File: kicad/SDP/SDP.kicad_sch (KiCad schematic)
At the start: 83 parts, among them J1 GPIO, J2 SPI, J24 POWER, J3 UART, J4 I2C, J5 Conn_01x04, J6 Conn_01x04, J7 RJ25, SW1 SW_Push, U1 TPS54233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

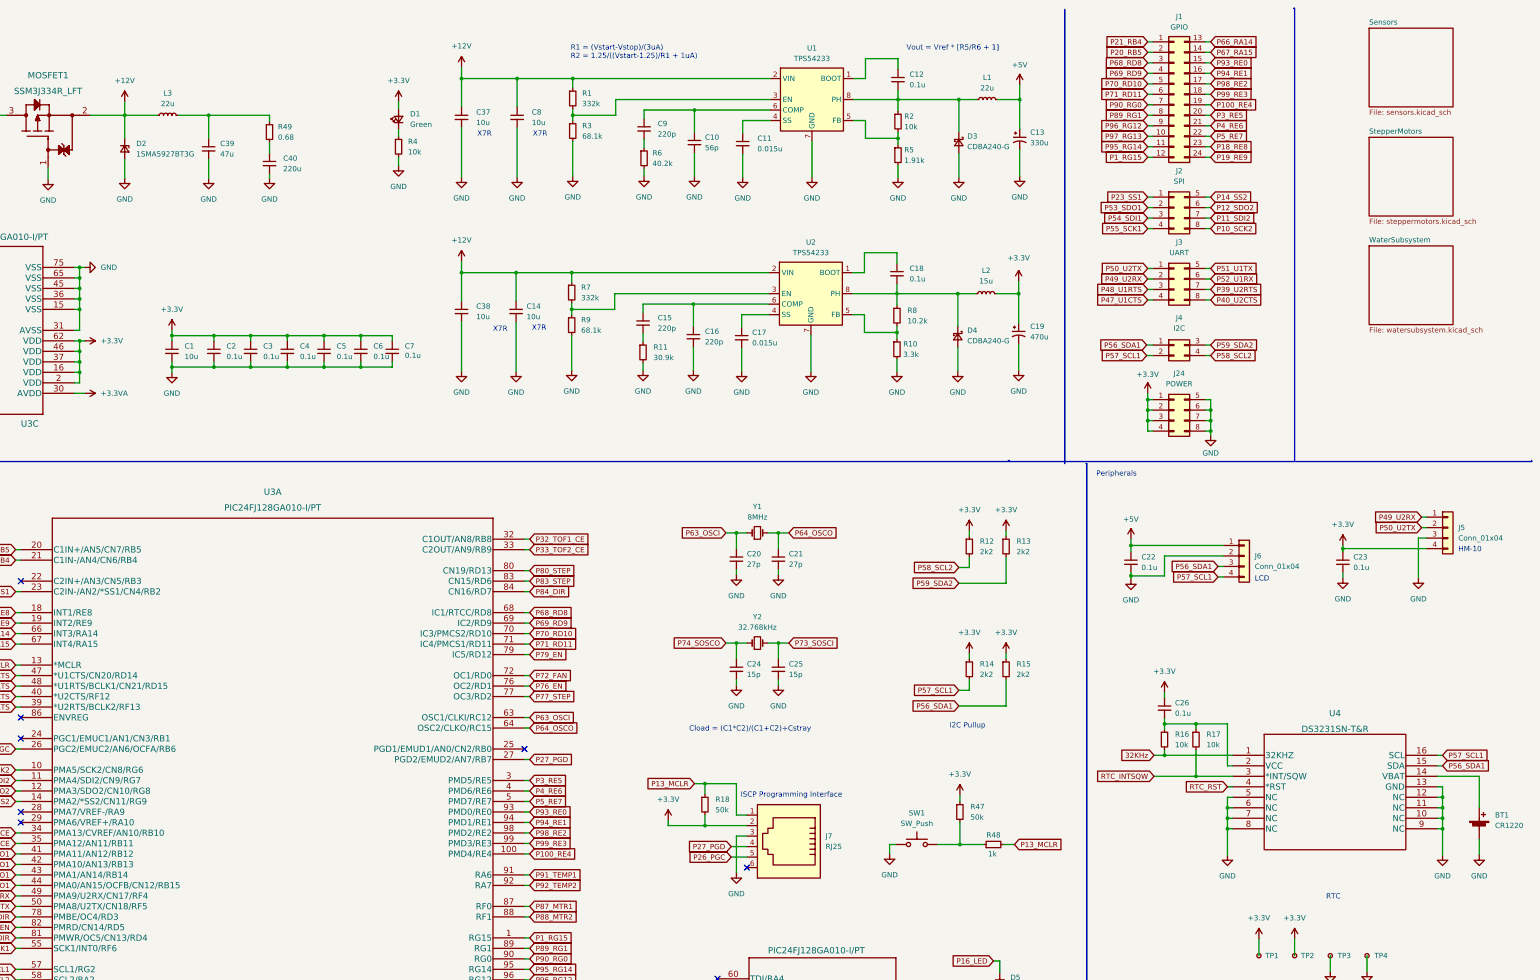
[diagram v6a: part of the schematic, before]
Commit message: PCB layout and footprint assignment fix
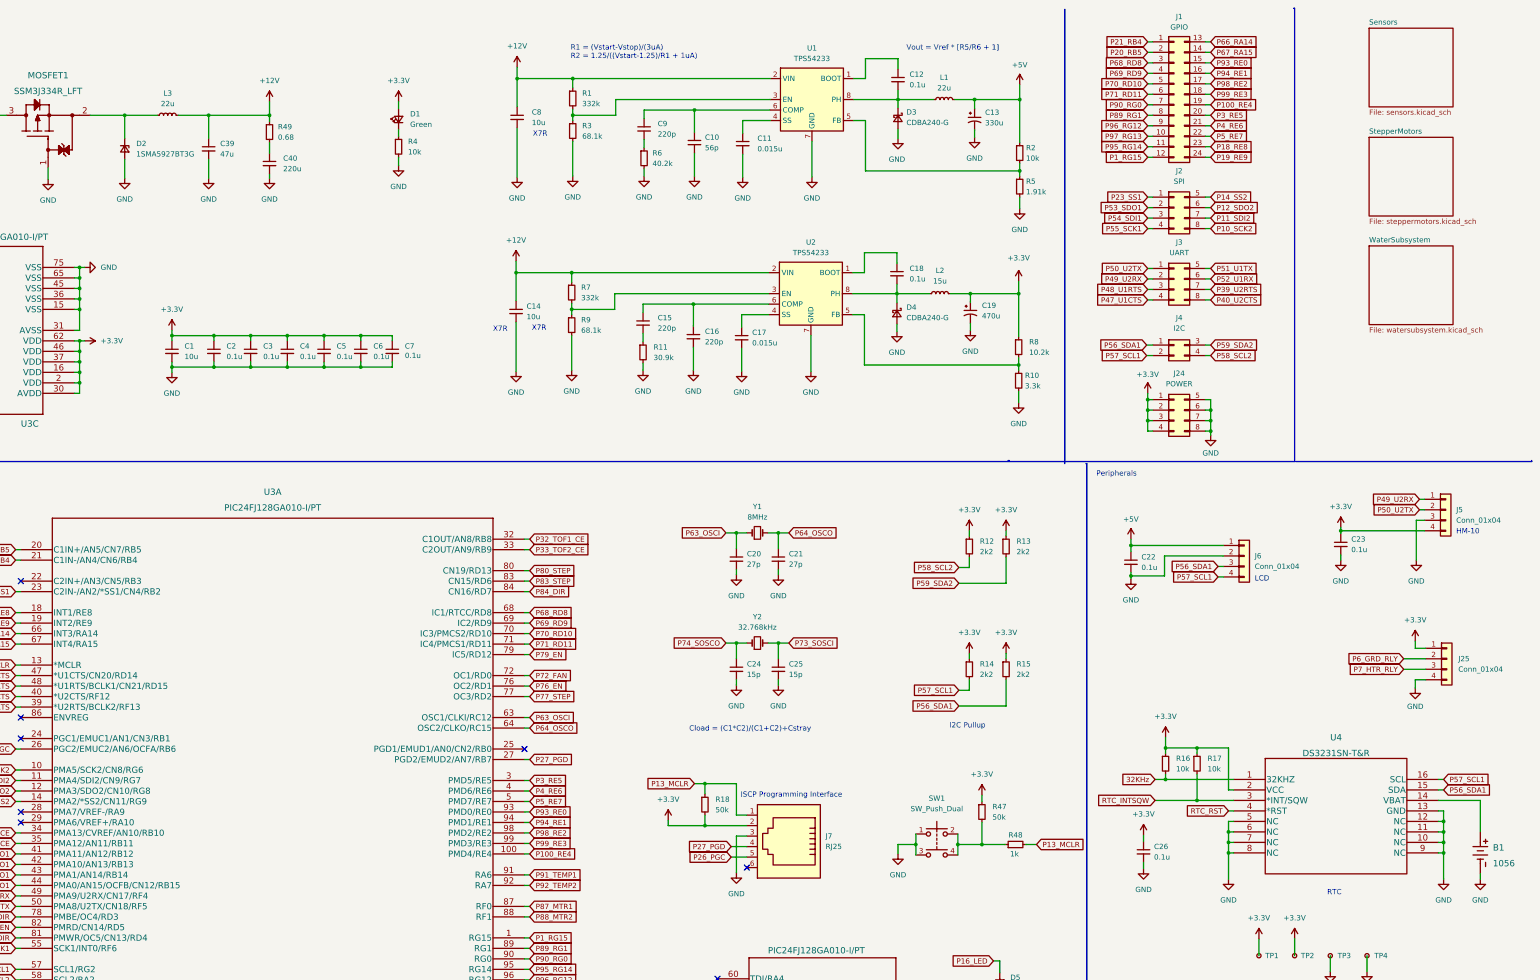
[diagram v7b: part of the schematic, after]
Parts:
- removed BT1: CR1220, Keystone_1056:1056, symbol Device:Battery_Cell
- removed C37, C38: 10u, Capacitor_SMD:C_1206_3216Metric, symbol Device:C_Small
- removed SW1: SW_Push, 1825910-6:SW_1825910-6-4, symbol Switch:SW_Push
- added B1: 1056, Keystone_1056:1056, symbol 2022-02-09_04-22-24:1056
- added J25: Conn_01x04, Connector_PinSocket_2.54mm:PinSocket_1x04_P2.54mm_Vertical, symbol Connector_Generic:Conn_01x04
- added SW1: SW_Push_Dual, 1825910-6:SW_1825910-6-4, symbol Switch:SW_Push_Dual
- J7: footprint 50TZV100M:50TZV100M8X10.5 -> 5555165-1:TE_5555165-1
- TP1, TP2, TP3, TP4: footprint (none) -> TestPoint:TestPoint_Pad_D2.0mm
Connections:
- net +3.3VA is gone; now on net +3V3: U3.30 (AVDD)
- net +12V: now also C39.1, L3.2, R49.1; no longer D2.1 (K), L3.1, MOSFET1.2 (SOURCE)
- net +3V3: now also R16.1, R17.1, R8.1, U4.2 (VCC), J25.1 (Pin_1)
- net +5V: now also R2.1
- net GND: now also C26.2, B1.1, J25.4 (Pin_4), SW1.1, SW1.3
- net P6_GRD_RLY: now also J25.2 (Pin_2)
- net P7_HTR_RLY: now also J25.3 (Pin_3)
- net at U4.14 (VBAT): now also B1.2
- net at C18.2, D4.1 (K), L2.1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: no longer R8.1
- net at C12.2, D3.1 (K), L1.1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: no longer R2.1
- net at R47.2, R48.1: now also SW1.2, SW1.4
- new net: D2.1 (K), L3.1, MOSFET1.2 (SOURCE)
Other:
- moved on the sheet: C13, C19, C23, C26, D3, D4, J5, L1, L2, R10, R16, R17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

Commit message: PCB layout and schematic updates
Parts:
- removed J1: GPIO, Connector_PinSocket_2.54mm:PinSocket_2x12_P2.54mm_Vertical, symbol Connector_Generic:Conn_02x12_Top_Bottom
- removed J2: SPI, Connector_PinSocket_2.54mm:PinSocket_2x04_P2.54mm_Vertical, symbol Connector_Generic:Conn_02x04_Top_Bottom
- removed J24: POWER, Connector_PinSocket_2.54mm:PinSocket_2x04_P2.54mm_Vertical, symbol Connector_Generic:Conn_02x04_Top_Bottom
- removed J3: UART, Connector_PinSocket_2.54mm:PinSocket_2x04_P2.54mm_Vertical, symbol Connector_Generic:Conn_02x04_Top_Bottom
- removed J4: I2C, Connector_PinSocket_2.54mm:PinSocket_2x02_P2.54mm_Vertical, symbol Connector_Generic:Conn_02x02_Top_Bottom
- added J1: GPIO, Connector_PinSocket_2.54mm:PinSocket_2x09_P2.54mm_Vertical, symbol Connector_Generic:Conn_02x09_Odd_Even
- added J2: SPI, Connector_PinSocket_2.54mm:PinSocket_2x04_P2.54mm_Vertical, symbol Connector_Generic:Conn_02x04_Odd_Even
- added J24: POWER, Connector_PinSocket_2.54mm:PinSocket_2x04_P2.54mm_Vertical, symbol Connector_Generic:Conn_02x04_Odd_Even
- added J26: Conn_01x02, TerminalBlock_Phoenix:TerminalBlock_Phoenix_PT-1,5-2-5.0-H_1x02_P5.00mm_Horizontal, symbol Connector_Generic:Conn_01x02
- added J3: UART, Connector_PinSocket_2.54mm:PinSocket_2x04_P2.54mm_Vertical, symbol Connector_Generic:Conn_02x04_Odd_Even
- added J4: I2C, Connector_PinSocket_2.54mm:PinSocket_2x02_P2.54mm_Vertical, symbol Connector_Generic:Conn_02x02_Odd_Even
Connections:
- net +3V3: now also J24.1 (Pin_1), J24.3 (Pin_3), J24.5 (Pin_5), J24.7 (Pin_7)
- net GND: now also J24.2 (Pin_2), J24.4 (Pin_4), J24.6 (Pin_6), J24.8 (Pin_8), J26.2 (Pin_2)
- net P10_SCK2: now also J2.8 (Pin_8)
- net P11_SDI2: now also J2.6 (Pin_6)
- net P12_SDO2: now also J2.4 (Pin_4)
- net P14_SS2: now also J2.2 (Pin_2)
- net P18_RE8: now also J1.2 (Pin_2)
- net P19_RE9: now also J1.1 (Pin_1)
- net P1_RG15: now also J1.5 (Pin_5)
- net P20_RB5: now also J1.4 (Pin_4)
- net P21_RB4: now also J1.3 (Pin_3)
- net P23_SS1: now also J2.1 (Pin_1)
- net P39_U2RTS: now also J3.6 (Pin_6)
- net P3_RE5: now also J1.6 (Pin_6)
- net P40_U2CTS: now also J3.8 (Pin_8)
- net P47_U1CTS: now also J3.7 (Pin_7)
- net P48_U1RTS: now also J3.5 (Pin_5)
- net P49_U2RX: now also J3.3 (Pin_3)
- net P4_RE6: now also J1.7 (Pin_7)
- net P50_U2TX: now also J3.1 (Pin_1)
- net P51_U1TX: now also J3.2 (Pin_2)
- net P52_U1RX: now also J3.4 (Pin_4)
- net P53_SDO1: now also J2.3 (Pin_3)
- net P54_SDI1: now also J2.5 (Pin_5)
- net P55_SCK1: now also J2.7 (Pin_7)
- net P56_SDA1: now also J4.1 (Pin_1)
- net P57_SCL1: now also J4.3 (Pin_3)
- net P58_SCL2: now also J4.4 (Pin_4)
- net P59_SDA2: now also J4.2 (Pin_2)
- net P5_RE7: now also J1.8 (Pin_8)
- net P66_RA14: now also J1.9 (Pin_9)
- net P67_RA15: now also J1.11 (Pin_11)
- net P68_RD8: now also J1.10 (Pin_10)
- net P69_RD9: now also J1.12 (Pin_12)
- net P70_RD10: now also J1.13 (Pin_13)
- net P71_RD11: now also J1.14 (Pin_14)
- net P89_RG1: now also J1.15 (Pin_15)
- net P90_RG0: now also J1.16 (Pin_16)
- net P93_RE0: now also J1.17 (Pin_17)
- net P94_RE1: now also J1.18 (Pin_18)
- net V_IN: now also J26.1 (Pin_1)
- net P100_RE4 renamed P100_LIMIT
- net P95_RG14 renamed P95_LIMIT
- net P96_RG12 renamed P96_LIMIT
- net P97_RG13 renamed P97_LIMIT
- net P98_RE2 renamed P98_LIMIT
- net P99_RE3 renamed P99_LIMIT
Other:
- moved on the sheet: C39, C40, D1, D2, F1, L3, MOSFET1, R4, R49
